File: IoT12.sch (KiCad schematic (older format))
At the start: 97 parts, among them J1 Conn_01x04_Male, Q1 2N7002, Q2 2N7002, Q3 AOD403, SW1 Rotary_Encoder_Switch, U1 MAX809S, U2 AT24C32, U3 INA826AID, U4 INA826AID, U5 ADS1115IDGS, U6 LM393, U7 74HC125, U8 LM2596S-ADJ

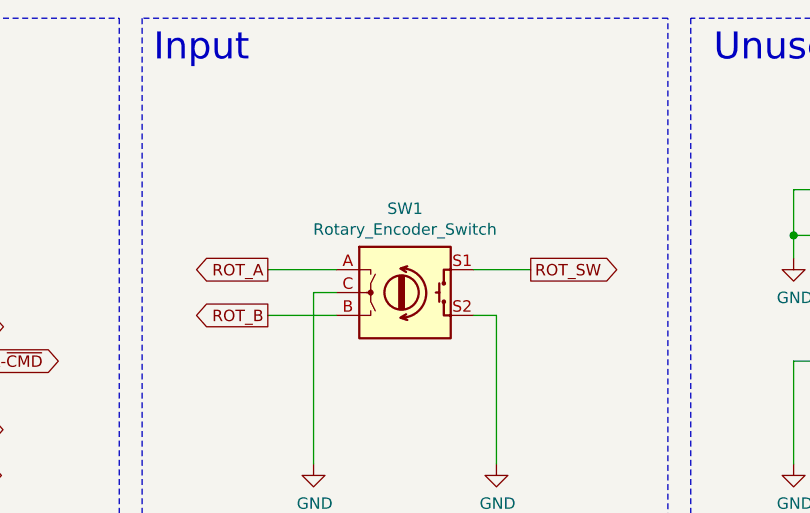
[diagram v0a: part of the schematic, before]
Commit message: Updated rotary encoder model#
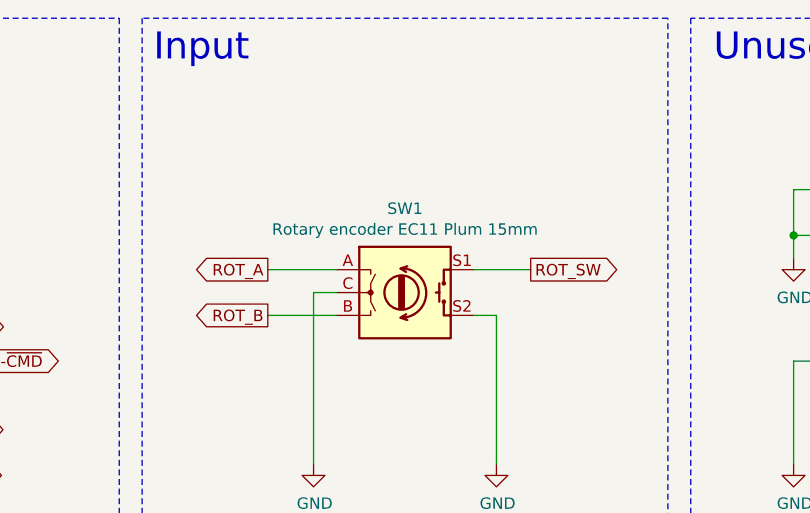
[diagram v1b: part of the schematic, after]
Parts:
- SW1: value Rotary_Encoder_Switch -> Rotary encoder EC11 Plum 15mm
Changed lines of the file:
@@
 P 13000 1750
 F 0 "SW1" H 13000 2117 50  0000 C CNN
-F 1 "Rotary_Encoder_Switch" H 13000 2026 50  0000 C CNN
+F 1 "Rotary encoder EC11 Plum 15mm" H 13000 2026 50  0000 C CNN
 F 2 "Rotary_Encoder-fixed:RotaryEncoder_Alps_EC11E-Switch_Vertical_H20mm_CircularMountingHoles" H 12850 1910 50  0001 C CNN
 F 3 "~" H 13000 2010 50  0001 C CNN

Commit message: PCB V1.1
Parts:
- added D8: BAV99, Package_TO_SOT_SMD:SOT-23, symbol Diode:BAV99
- A1: value ESP32-DevKitC -> 2x Conn_01x19_Female; Description (none) -> ESP32-DevKitC
- A2: value Nokia_5110_display -> 2x Conn_01x09_Female; Description (none) -> Nokia_5110_display
- LS1: value Piezo disc -> Conn_01x02_Male; Description (none) -> Piezo disc
- R10: value 220R 1% -> 470R 1%
- R11: value 470R 1% -> 1k 1%
- R24, R25, R26, R27, R28: value 10k 1% -> 10k 0.1%
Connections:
- net at U1.2 (~RESET): now also D8.2 (A), D8.3 (K); no longer R2.2
- net VADC renamed VIN
- net Vin: no longer names the net of F1.2, F2.2, J101.1 (Pin_1)
- new net: D8.1 (K), R2.2
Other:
- note added: "0.005V@1A\n0.015V@3A\n0.025V@5A"
- note added: "0.756V@3A"
- note added: "0.92V@500°C"
- note added: "50.4G"
- note added: "8.657mV@500°C\n(Tamb = 0°C)"
- note added: "Keep output \nunder 1V at \nfull scale input."
- note added: "Matched*"
- note added: "Matched*: value does not matter that much, \nbut resistors must be matched to equal value.\nYou may use oridinary 5% resitors and \ncherry-pick a perfectly equal pair."
- note added: "VADC = \nVin*0.0449"
- note removed: "0.015V@3A"
- note removed: "1.5915V@3A"
- note removed: "1.952V@500°C"
- note removed: "225.5G"
- note removed: "8.657mV@500°C"
- note removed: "Matched"
- moved on the sheet: R2, U1
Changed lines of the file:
@@
 L power:+3.3V #PWR0122
 U 1 1 5FF16F22
-P 14550 3650
-F 0 "#PWR0122" H 14550 3500 50  0001 C CNN
-F 1 "+3.3V" H 14565 3823 50  0000 C CNN
-F 2 "" H 14550 3650 50  0001 C CNN
-F 3 "" H 14550 3650 50  0001 C CNN
-	1    14550 3650
+P 14450 3650
+F 0 "#PWR0122" H 14450 3500 50  0001 C CNN
+F 1 "+3.3V" H 14465 3823 50  0000 C CNN
+F 2 "" H 14450 3650 50  0001 C CNN
+F 3 "" H 14450 3650 50  0001 C CNN
+	1    14450 3650
 	1    0    0    -1
 $EndComp
@@
 L power:GND #PWR0126
 U 1 1 5FF173EA
-P 14550 4450
-F 0 "#PWR0126" H 14550 4200 50  0001 C CNN
-F 1 "GND" H 14555 4277 50  0000 C CNN
-F 2 "" H 14550 4450 50  0001 C CNN
-F 3 "" H 14550 4450 50  0001 C CNN
-	1    14550 4450
-	1    0    0    -1
-$EndComp
-Wire Wire Line
-	14550 4350 14550 4450
-Wire Wire Line
-	14550 3650 14550 3750
-Wire Wire Line
-	15500 4050 15600 4050
-Text GLabel 15600 4050 2    50   Output ~ 0
-~RESET
+P 14450 4450
+F 0 "#PWR0126" H 14450 4200 50  0001 C CNN
+F 1 "GND" H 14455 4277 50  0000 C CNN
+F 2 "" H 14450 4450 50  0001 C CNN
+F 3 "" H 14450 4450 50  0001 C CNN
+	1    14450 4450
+	1    0    0    -1
+$EndComp
+Wire Wire Line
+	14450 4350 14450 4450
+Wire Wire Line
+	14450 3650 14450 3750
 Text GLabel 9050 1700 0    50   Input ~ 0
 ~RESET
@@
 Wire Wire Line
 	12450 4000 12200 4000
-Text Label 1200 1750 0    50   ~ 0
-Vin
 $Comp
 L Mechanical:MountingHole H3
@@
 U 1 1 607BA4F0
 P 8400 2350
-F 0 "LS1" H 8366 2667 50  0000 C CNN
-F 1 "Piezo disc" H 8366 2576 50  0000 C CNN
+F 0 "LS1" H 8575 2391 50  0000 L CNN
+F 1 "Conn_01x02_Male" H 8575 2300 50  0000 L CNN
 F 2 "Connector_PinHeader_2.54mm:PinHeader_1x02_P2.54mm_Vertical" H 8365 2300 50  0001 C CNN
 F 3 "~" H 8365 2300 50  0001 C CNN
+F 4 "Piezo disc" H 8575 2209 50  0000 L CNN "Description"
 	1    8400 2350
 	-1   0    0    -1
@@
 P 3300 5500
 F 0 "A2" H 3500 5950 50  0000 L CNN
-F 1 "Nokia_5110_display" H 2900 4750 50  0000 L CNN
+F 1 "2x Conn_01x09_Female" H 2800 4750 50  0000 L CNN
 F 2 "Display-extra:Nokia_5110_display_module" H 3300 4900 50  0001 C CNN
 F 3 "" H 3700 5200 50  0001 C CNN
+F 4 "Nokia_5110_display" H 3250 4650 50  0000 C CNN "Description"
 	1    3300 5500
 	1    0    0    -1
@@
 $EndComp
 $Comp
-L Device:R R2
-U 1 1 5FF18CDB
-P 15350 4050
-F 0 "R2" V 15143 4050 50  0000 C CNN
-F 1 "100R" V 15234 4050 50  0000 C CNN
-F 2 "Resistor_SMD:R_0805_2012Metric_Pad1.20x1.40mm_HandSolder" V 15280 4050 50  0001 C CNN
-F 3 "~" H 15350 4050 50  0001 C CNN
-	1    15350 4050
-	0    1    1    0
-$EndComp
-$Comp
 L Power_Supervisor:TPS3839DBZ U1
 U 1 1 5FF16B0D
-P 14550 4050
-F 0 "U1" H 14850 4350 50  0000 R CNN
-F 1 "MAX809S" H 14900 3800 50  0000 R CNN
-F 2 "Package_TO_SOT_SMD:SOT-23" H 14550 4050 50  0001 C CNN
-F 3 "" H 14550 4050 50  0001 C CNN
-	1    14550 4050
+P 14450 4050
+F 0 "U1" H 14750 4350 50  0000 R CNN
+F 1 "MAX809S" H 14800 3800 50  0000 R CNN
+F 2 "Package_TO_SOT_SMD:SOT-23" H 14450 4050 50  0001 C CNN
+F 3 "" H 14450 4050 50  0001 C CNN
+	1    14450 4050
 	1    0    0    -1
 $EndComp
@@
 P 9950 2750
 F 0 "A1" H 10450 4000 50  0000 C CNN
-F 1 "ESP32-DevKitC" H 10300 1000 50  0000 C CNN
+F 1 "2x Conn_01x19_Female" H 10450 1000 50  0000 C CNN
 F 2 "Module-extra:ESP32-DevKitC" H 9950 850 50  0001 C CNN
 F 3 "https://www.espressif.com/sites/default/files/documentation/esp32-wroom-32_datasheet_en.pdf" H 9650 2650 50  0001 C CNN
+F 4 "ESP32-DevKitC" H 10300 900 50  0000 C CNN "Description"
 	1    9950 2750
 	1    0    0    -1
@@
 	2050 2500 2050 2700
 Text GLabel 2150 2500 2    50   Output ~ 0
-VADC
+VIN
 Wire Wire Line
 	2050 2500 2150 2500
 Text GLabel 4700 5750 0    50   Input ~ 0
-VADC
+VIN
 Wire Notes Line
 	11750 7500 7000 7500
@@
 P 12800 6100
 F 0 "R25" V 12593 6100 50  0000 C CNN
-F 1 "10k 1%" V 12684 6100 50  0000 C CNN
+F 1 "10k 0.1%" V 12684 6100 50  0000 C CNN
 F 2 "Resistor_SMD:R_0805_2012Metric_Pad1.20x1.40mm_HandSolder" V 12730 6100 50  0001 C CNN
 F 3 "~" H 12800 6100 50  0001 C CNN
@@
 P 13650 6450
 F 0 "R11" H 13720 6404 50  0000 L CNN
-F 1 "470R 1%" H 13720 6495 50  0000 L CNN
+F 1 "1k 1%" H 13720 6495 50  0000 L CNN
 F 2 "Resistor_SMD:R_0805_2012Metric_Pad1.20x1.40mm_HandSolder" V 13580 6450 50  0001 C CNN
 F 3 "~" H 13650 6450 50  0001 C CNN
@@
 Wire Wire Line
 	13750 6600 13650 6600
-Text Notes 13300 6650 0    50   ~ 0
-106.1G
+Text Notes 13350 6650 0    50   ~ 0
+50.4G
 Wire Wire Line
 	14300 6750 14300 6900
@@
 P 12800 6800
 F 0 "R26" V 12593 6800 50  0000 C CNN
-F 1 "10k 1%" V 12684 6800 50  0000 C CNN
+F 1 "10k 0.1%" V 12684 6800 50  0000 C CNN
 F 2 "Resistor_SMD:R_0805_2012Metric_Pad1.20x1.40mm_HandSolder" V 12730 6800 50  0001 C CNN
 F 3 "~" H 12800 6800 50  0001 C CNN
@@
 P 12800 9250
 F 0 "R28" V 12593 9250 50  0000 C CNN
-F 1 "10k 1%" V 12684 9250 50  0000 C CNN
+F 1 "10k 0.1%" V 12684 9250 50  0000 C CNN
 F 2 "Resistor_SMD:R_0805_2012Metric_Pad1.20x1.40mm_HandSolder" V 12730 9250 50  0001 C CNN
 F 3 "~" H 12800 9250 50  0001 C CNN
@@
 P 12800 8550
 F 0 "R27" V 12593 8550 50  0000 C CNN
-F 1 "10k 1%" V 12684 8550 50  0000 C CNN
+F 1 "10k 0.1%" V 12684 8550 50  0000 C CNN
 F 2 "Resistor_SMD:R_0805_2012Metric_Pad1.20x1.40mm_HandSolder" V 12730 8550 50  0001 C CNN
 F 3 "~" H 12800 8550 50  0001 C CNN
@@
 	12600 8100 12600 9350
 Text Notes 12650 8200 0    50   ~ 0
-Matched
+Matched*
 Text Notes 12650 5750 0    50   ~ 0
-Matched
+Matched*
 Wire Notes Line
 	13000 6900 12600 6900
@@
 Wire Wire Line
 	4050 9000 4050 10100
-Wire Wire Line
-	14950 4050 15200 4050
 Wire Wire Line
 	5000 9850 5000 10200
@@
 Wire Wire Line
 	10650 10150 10950 10150
-Text Notes 11950 6500 0    50   ~ 0
-0.015V@3A
+Text Notes 11950 6550 0    50   ~ 0
+0.005V@1A\n0.015V@3A\n0.025V@5A
 $Comp
 L Analog_ADC:ADS1115IDGS U5
@@
 	14500 9200 14500 9350
 Text Notes 13500 9100 0    50   ~ 0
-225.5G
+106.1G
 Wire Wire Line
 	13950 9050 13850 9050
@@
 P 13850 8900
 F 0 "R10" H 13920 8854 50  0000 L CNN
-F 1 "220R 1%" H 13920 8945 50  0000 L CNN
+F 1 "470R 1%" H 13920 8945 50  0000 L CNN
 F 2 "Resistor_SMD:R_0805_2012Metric_Pad1.20x1.40mm_HandSolder" V 13780 8900 50  0001 C CNN
 F 3 "~" H 13850 8900 50  0001 C CNN
@@
 	1    0    0    -1
 $EndComp
-Text Notes 15350 6350 0    50   ~ 0
-1.5915V@3A
 $Comp
 L Device:C C4
@@
 	1    0    0    -1
 $EndComp
-Text Notes 11950 8900 0    50   ~ 0
-8.657mV@500°C
+Text Notes 11900 8950 0    50   ~ 0
+8.657mV@500°C\n(Tamb = 0°C)
 Text Notes 15350 8800 0    50   ~ 0
-1.952V@500°C
+0.92V@500°C
 Text Notes 13650 4650 0    50   ~ 0
 1.65V@25°C
@@
 P 13350 3950
 F 0 "R24" H 13420 3996 50  0000 L CNN
-F 1 "10k 1%" H 13420 3905 50  0000 L CNN
+F 1 "10k 0.1%" H 13420 3905 50  0000 L CNN
 F 2 "Resistor_SMD:R_0805_2012Metric_Pad1.20x1.40mm_HandSolder" V 13280 3950 50  0001 C CNN
 F 3 "~" H 13350 3950 50  0001 C CNN
@@
 Text Label 10300 9900 0    50   ~ 0
 IRON_-
+Text Notes 11950 9750 0    50   ~ 0
+Matched*: value does not matter that much, \nbut resistors must be matched to equal value.\nYou may use oridinary 5% resitors and \ncherry-pick a perfectly equal pair.
+Text Notes 1600 2600 0    50   ~ 0
+VADC = \nVin*0.0449
+Text Notes 15300 8650 0    50   ~ 0
+Keep output \nunder 1V at \nfull scale input.
+Text Notes 15300 6200 0    50   ~ 0
+Keep output \nunder 1V at \nfull scale input.
+Text Notes 15350 6350 0    50   ~ 0
+0.756V@3A
+$Comp
+L Diode:BAV99 D8
+U 1 1 6021EFB1
+P 14900 4350
+F 0 "D8" V 14850 4200 50  0000 L CNN
+F 1 "BAV99" V 14750 4050 50  0000 L CNN
+F 2 "Package_TO_SOT_SMD:SOT-23" H 14900 3850 50  0001 C CNN
+F 3 "https://assets.nexperia.com/documents/data-sheet/BAV99_SER.pdf" H 14900 4350 50  0001 C CNN
+	1    14900 4350
+	0    -1   -1   0
+$EndComp
+Wire Wire Line
+	14850 4050 14900 4050
+$Comp
+L Device:R R2
+U 1 1 5FF18CDB
+P 15400 4050
+F 0 "R2" V 15193 4050 50  0000 C CNN
+F 1 "100R" V 15284 4050 50  0000 C CNN
+F 2 "Resistor_SMD:R_0805_2012Metric_Pad1.20x1.40mm_HandSolder" V 15330 4050 50  0001 C CNN
+F 3 "~" H 15400 4050 50  0001 C CNN
+	1    15400 4050
+	0    1    1    0
+$EndComp
+Text GLabel 15600 4050 2    50   Output ~ 0
+~RESET
+Wire Wire Line
+	15550 4050 15600 4050
+Wire Wire Line
+	15100 4350 15100 4050
+Wire Wire Line
+	15100 4050 14900 4050
+Connection ~ 14900 4050
+Wire Wire Line
+	14900 4650 15250 4650
+Wire Wire Line
+	15250 4650 15250 4050
 $EndSCHEMATC

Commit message: Updated schematic and pcb.
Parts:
- added D10, D9: BAV99, Package_TO_SOT_SMD:SOT-23, symbol Diode:BAV99
- C2, C3, C4, C5: value 10nF -> 1nF
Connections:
- net GND: now also D10.2 (A), D10.3 (K), D9.2 (A), D9.3 (K)
- net at C4.2, R28.1, U4.1 (-): now also D9.1 (K)
- net at C4.1, R27.1, U4.4 (+): now also D10.1 (K)
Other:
- note added: "This space \nfor rent."
- moved on the sheet: C10, C2, C3, C4, C5, C9, D3, D4, D7, NT2, NT3, Q2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

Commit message: Schematic split into multiple sheets.
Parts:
- removed A1: 2x Conn_01x19_Female, Module-extra:ESP32-DevKitC, symbol MCU_Module-extra:ESP32-DevKitC
- removed A2: 2x Conn_01x09_Female, Display-extra:Nokia_5110_display_module, symbol Display_Graphic-extra:Nokia_5110_display
- removed C1: 100pF, Capacitor_SMD:C_0805_2012Metric_Pad1.18x1.45mm_HandSolder, symbol Device:C
- removed C10, C11, C12, C13, C6, C7, C8, C9: 100nF, Capacitor_SMD:C_0805_2012Metric_Pad1.18x1.45mm_HandSolder, symbol Device:C
- removed C14: 10uF, Capacitor_SMD:C_0805_2012Metric_Pad1.18x1.45mm_HandSolder, symbol Device:C
- removed C15, C16: 100uF/35V, Capacitor_SMD:CP_Elec_6.3x7.7, symbol Device:CP
- removed C2, C3, C4, C5: 1nF, Capacitor_SMD:C_0805_2012Metric_Pad1.18x1.45mm_HandSolder, symbol Device:C
- removed D1: Red, LED_SMD:LED_0805_2012Metric_Pad1.15x1.40mm_HandSolder, symbol Device:LED
- removed D10, D2, D8, D9: BAV99, Package_TO_SOT_SMD:SOT-23, symbol Diode:BAV99
- removed D3: BZX84C18, Diode_SMD:D_SOT-23_ANK, symbol Diode:BZX84Cxx
- removed D4: SS14, Diode_SMD:D_SMA, symbol Device:D_Schottky
- removed D5, D6, D7: SS34, Diode_SMD:D_SMA, symbol Device:D_Schottky
- removed F1: 0.5A/30V, Fuse:Fuse_Bourns_MF-RG400, symbol Device:Polyfuse
- removed F2: 2.5A/30V, Fuse:Fuse_Bourns_MF-RG1000, symbol Device:Polyfuse
- removed J1: Conn_01x04_Male, Connector_PinHeader_2.54mm:PinHeader_1x06_P2.54mm_Vertical, symbol Connector:Conn_01x06_Male
- removed J101, J102, J103, J105, J106, J107, J108, J109: ~, TestPoint:TestPoint_THTPad_D2.0mm_Drill1.0mm, symbol Connector_Generic:Conn_01x01
- removed L1: 68uH, Inductor_SMD:L_12x12mm_H8mm, symbol Device:L
- removed LS1: Conn_01x02_Male, Connector_PinHeader_2.54mm:PinHeader_1x02_P2.54mm_Vertical, symbol Device:Speaker_Crystal
- removed NT1, NT2, NT3: ~, NetTie-extra:NetTie-2_SMD_Pad0.25mm, symbol Device:Net-Tie_2
- removed Q1, Q2: 2N7002, Package_TO_SOT_SMD:SOT-23, symbol Transistor_FET:2N7002
- removed Q3: AOD403, Package_TO_SOT_SMD:TO-252-2, symbol Transistor_FET-extra:AOD403
- removed R1: 0R005, Resistor_SMD:R_2512_6332Metric_Pad1.52x3.35mm_HandSolder, symbol Device:R
- removed R10: 470R 1%, Resistor_SMD:R_0805_2012Metric_Pad1.20x1.40mm_HandSolder, symbol Device:R
- removed R11: 1k 1%, Resistor_SMD:R_0805_2012Metric_Pad1.20x1.40mm_HandSolder, symbol Device:R
- removed R12, R13: 1k, Resistor_SMD:R_0805_2012Metric_Pad1.20x1.40mm_HandSolder, symbol Device:R
- removed R14: 3k3, Resistor_SMD:R_0805_2012Metric_Pad1.20x1.40mm_HandSolder, symbol Device:R
- removed R15, R16, R17, R18, R19, R20, R21: 4k7, Resistor_SMD:R_0805_2012Metric_Pad1.20x1.40mm_HandSolder, symbol Device:R
- removed R2, R3, R4, R5, R6, R7, R8, R9: 100R, Resistor_SMD:R_0805_2012Metric_Pad1.20x1.40mm_HandSolder, symbol Device:R
- removed R23, R29: 10k, Resistor_SMD:R_0805_2012Metric_Pad1.20x1.40mm_HandSolder, symbol Device:R
- removed R24, R25, R26, R27, R28: 10k 0.1%, Resistor_SMD:R_0805_2012Metric_Pad1.20x1.40mm_HandSolder, symbol Device:R
- removed R30: 33k, Resistor_SMD:R_0805_2012Metric_Pad1.20x1.40mm_HandSolder, symbol Device:R
- removed R31, R32, R33, R34, R35, R36, R37: 100k, Resistor_SMD:R_0805_2012Metric_Pad1.20x1.40mm_HandSolder, symbol Device:R
- removed R38, R39, R40, R41: 1M, Resistor_SMD:R_0805_2012Metric_Pad1.20x1.40mm_HandSolder, symbol Device:R
- removed SW1: Rotary encoder EC11 Plum 15mm, Rotary_Encoder-fixed:RotaryEncoder_Alps_EC11E-Switch_Vertical_H20mm_CircularMountingHoles, symbol Device:Rotary_Encoder_Switch
- removed U1: MAX809S, Package_TO_SOT_SMD:SOT-23, symbol Power_Supervisor:TPS3839DBZ
- removed U2: AT24C32, Package_SO:SO-8_3.9x4.9mm_P1.27mm, symbol Memory_EEPROM:24LC32
- removed U3, U4: INA826AID, Package_SO:SOIC-8_3.9x4.9mm_P1.27mm, symbol Amplifier_Instrumentation-extra:INA826
- removed U5: ADS1115IDGS, Package_SO:TSSOP-10_3x3mm_P0.5mm, symbol Analog_ADC:ADS1115IDGS
- removed U6: LM393, Package_SO:SO-8_3.9x4.9mm_P1.27mm, symbol Comparator:LM393
- removed U7: 74HC125, Package_SO:SOIC-14_3.9x8.7mm_P1.27mm, symbol 74xx:74LS125
- removed U8: LM2596S-ADJ, Package_TO_SOT_SMD:TO-263-5_TabPin3, symbol Regulator_Switching:LM2596S-ADJ
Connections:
- no-connect marks 21 -> 0
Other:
- note removed: "0.005V@1A\n0.015V@3A\n0.025V@5A"
- note removed: "0.756V@3A"
- note removed: "0.92V@500°C"
- note removed: "1.65V@25°C"
- note removed: "106.1G"
- note removed: "50.4G"
- note removed: "8.657mV@500°C\n(Tamb = 0°C)"
- note removed: "About 0.5s timeout \nafter PWM fail \n(equal to 100% dutycycle) \nto switch off output."
- note removed: "Brainz, wireless brainz."
- note removed: "Display"
- note removed: "Expansion"
- note removed: "External 16b I2C ADC"
- note removed: "Handle NTC"
- note removed: "Heater PWM failsafe"
- note removed: "Heater power"
- note removed: "Heater power sensor"
- note removed: "Heater temperature sensor"
- note removed: "I2C: 0x48"
- note removed: "I2C: 0xA0"
- note removed: "Input"
- note removed: "Keep output \nunder 1V at \nfull scale input."
- note removed: "Matched*"
- note removed: "Matched*: value does not matter that much, \nbut resistors must be matched to equal value.\nYou may use oridinary 5% resitors and \ncherry-pick a perfectly equal pair."
- note removed: "Max 24V DC"
- note removed: "NTC"
- note removed: "Power supply"
- note removed: "Shake"
- note removed: "This space \nfor rent."
- note removed: "Tilt switch sensor as shake sensor"
- note removed: "Unused"
- note removed: "VADC = \nVin*0.0449"
- note removed: "Voltage monitor"
- moved on the sheet: H1, H2, H3, H4

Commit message: V2.0 pcb.
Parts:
- renumbered H3 to H2, H2 to H3
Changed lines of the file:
@@
 Sheet 1 5
 Title "IoT12-hardware"
-Date "2021-02-13"
-Rev "V1.1"
+Date "2021-02-21"
+Rev "V2.0"
 Comp ""
 Comment1 ""
@@
 $EndDescr
 $Comp
-L Mechanical:MountingHole H3
+L Mechanical:MountingHole H2
 U 1 1 5FF628B9
 P 1400 7350
-F 0 "H3" H 1500 7396 50  0000 L CNN
+F 0 "H2" H 1500 7396 50  0000 L CNN
 F 1 "MountingHole" H 1500 7305 50  0000 L CNN
 F 2 "MountingHole:MountingHole_3.2mm_M3_Pad_Via" H 1400 7350 50  0001 C CNN
@@
 $EndComp
 $Comp
-L Mechanical:MountingHole H2
+L Mechanical:MountingHole H3
 U 1 1 5FF62514
 P 650 7600
-F 0 "H2" H 750 7646 50  0000 L CNN
+F 0 "H3" H 750 7646 50  0000 L CNN
 F 1 "MountingHole" H 750 7555 50  0000 L CNN
 F 2 "MountingHole:MountingHole_3.2mm_M3_Pad_Via" H 650 7600 50  0001 C CNN
